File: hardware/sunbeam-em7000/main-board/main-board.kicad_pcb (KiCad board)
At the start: 4 copper layers, 131 x 125 mm, 0 parts

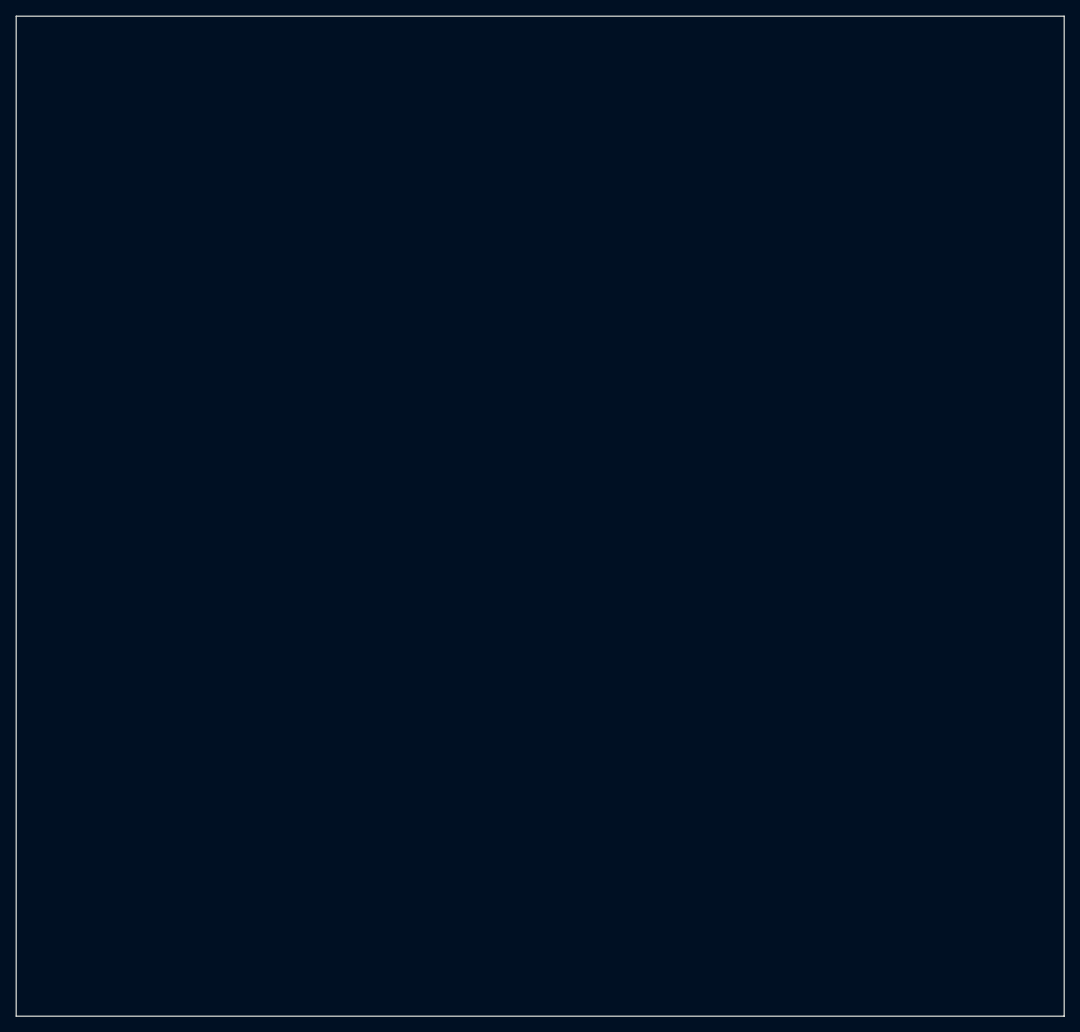
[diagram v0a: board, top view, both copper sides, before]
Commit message: main-board: placement candidate 1 [SOL-HW-MAIN-BOARD-PROVEN-AND-LAID-OUT.C7, .C18]
The first board branch's chosen placement (its candidate 5, 2f172f3a: candidate 4's mains-side moves and
TP202 at (71.5, 113.75)) replayed on this branch's floorplan, with the pump triacs T701 and T711 on the
board's two-lead DPAK land main-board:TO-252-2_TabPin2_Triac (swapped by KiCad's Python, keeping position,
turn, side, symbol link, fields and every pad's net, pin type and function; refilled and saved twice,
byte-identical). Every other footprint is the earlier board's, byte for byte in content.

Recorded as a candidate, not to be chosen: on the corrected floorplan the zero-crossing parts it leaves in
the old island (U602, R630, R631, TP103) stand in digital, outside the regions that list them.

The separation basis follows the land in the same commit (C18): the four entries that excused the 1.08 mm
gap of a middle-lead pad 2 against pads 1 and 3 are removed, since the land has no such pad; the tab pad
stands 2.00 mm from each lead pad, which meets the 2.0 mm terminal clearance and falls short of the 2.6 mm
creepage, so four creepage between entries at 2.0 mm take their place, unsigned (accepted_by and
accepted_on empty). The record's land and pin-distance comments, the division record's two restatements
and the record tests that pinned the 1.08 mm entries are brought to the land.

Co-Authored-By: Claude Sonnet 5.5 <noreply@anthropic.com>
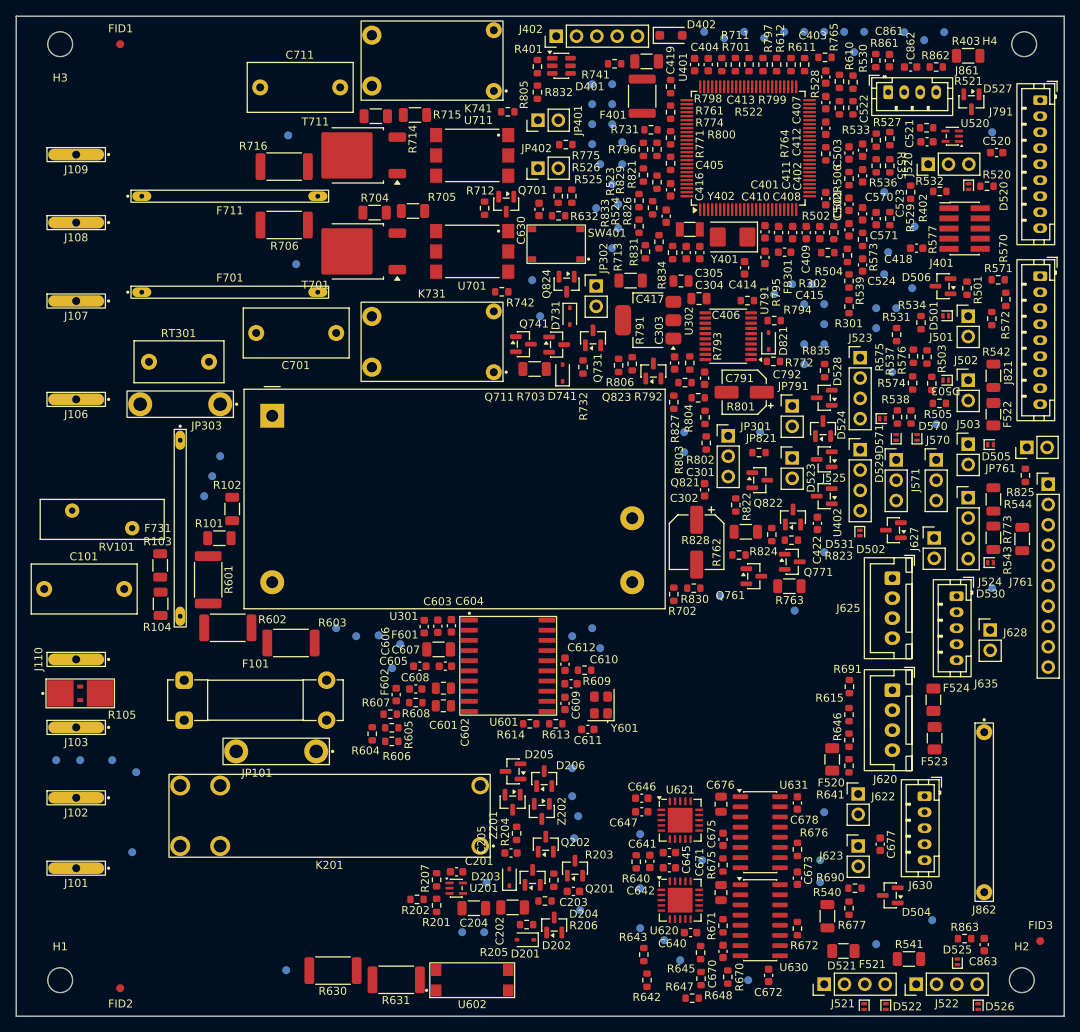
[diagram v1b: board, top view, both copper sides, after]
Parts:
- added C101: 100nF_X2, Capacitor_THT:C_Rect_L13.0mm_W6.0mm_P10.00mm_FKS3_FKP3_MKS4, F.Cu at (14.5, 73.6)
- added C201: 100n, Capacitor_SMD:C_0603_1608Metric, F.Cu at (56.0, 109.0)
- added C202: 100n, Capacitor_SMD:C_1206_3216Metric, F.Cu at (63.0, 113.4)
- added C203: 4.7n, Capacitor_SMD:C_0603_1608Metric, F.Cu at (70.7, 111.4)
- added C204: 100n, Capacitor_SMD:C_1206_3216Metric, F.Cu at (58.2, 113.5)
- added C205: 4.7n, Capacitor_SMD:C_0603_1608Metric, F.Cu at (62.9, 106.6)
- added C301: 100 nF, Capacitor_SMD:C_0603_1608Metric, F.Cu at (87.0, 61.2)
- added C302: 47 uF, Capacitor_SMD:CP_Elec_6.3x5.2, F.Cu at (86.0, 67.8)
- added C303: 10 uF, Capacitor_SMD:C_0603_1608Metric, F.Cu at (83.3, 45.4)
- added C304: 22 uF, Capacitor_SMD:C_0805_2012Metric, F.Cu at (86.3, 37.3)
- added C305: 22 uF, Capacitor_SMD:C_0805_2012Metric, F.Cu at (84.1, 35.1)
- added C401: 100 nF, Capacitor_SMD:C_0603_1608Metric, F.Cu at (94.6, 28.9)
- added C402: 100 nF, Capacitor_SMD:C_0603_1608Metric, F.Cu at (102.2, 24.8)
- added C403: 100 nF, Capacitor_SMD:C_0603_1608Metric, F.Cu at (102.2, 9.60)
- added C404: 100 nF, Capacitor_SMD:C_0603_1608Metric, F.Cu at (85.8, 8.05)
- added C405: 100 nF, Capacitor_SMD:C_0603_1608Metric, F.Cu at (82.8, 23.7)
- added C406: 100 nF, Capacitor_SMD:C_0603_1608Metric, F.Cu at (86.5, 31.6)
- added C407: 4.7 uF, Capacitor_SMD:C_0603_1608Metric, F.Cu at (102.2, 12.8)
- added C408: 100 nF, Capacitor_SMD:C_0603_1608Metric, F.Cu at (101.5, 29.1)
- added C409: 1 uF, Capacitor_SMD:C_0603_1608Metric, F.Cu at (99.8, 29.1)
- added C410: 100 nF, Capacitor_SMD:C_0603_1608Metric, F.Cu at (98.0, 29.1)
- added C411: 1 uF, Capacitor_SMD:C_0603_1608Metric, F.Cu at (96.3, 29.1)
- added C412: 2.2 uF, Capacitor_SMD:C_0603_1608Metric, F.Cu at (102.2, 16.0)
- added C413: 2.2 uF, Capacitor_SMD:C_0603_1608Metric, F.Cu at (87.5, 8.05)
- added C414: 20 pF, Capacitor_SMD:C_0603_1608Metric, F.Cu at (92.0, 33.5)
- added C415: 20 pF, Capacitor_SMD:C_0603_1608Metric, F.Cu at (94.6, 32.1)
- added C416: 4.7 pF, Capacitor_SMD:C_0603_1608Metric, F.Cu at (82.2, 27.0)
- added C417: 4.7 pF, Capacitor_SMD:C_0603_1608Metric, F.Cu at (84.8, 31.6)
- added C418: 100 nF, Capacitor_SMD:C_0603_1608Metric, F.Cu at (113.5, 31.0)
- added C419: 4.7 nF, Capacitor_SMD:C_1206_3216Metric, F.Cu at (79.8, 7.65)
- added C422: 100 nF, Capacitor_SMD:C_0603_1608Metric, F.Cu at (101.2, 65.4)
- added C501: 47n, Capacitor_SMD:C_0603_1608Metric, F.Cu at (105.1, 25.5)
- added C502: 47n, Capacitor_SMD:C_0603_1608Metric, F.Cu at (105.1, 28.7)
- added C503: 47n, Capacitor_SMD:C_0603_1608Metric, F.Cu at (105.1, 19.1)
- added C520: 47n, Capacitor_SMD:C_0603_1608Metric, F.Cu at (123.5, 19.1)
- added C521: 100n, Capacitor_SMD:C_0603_1608Metric, F.Cu at (114.8, 17.7)
- added C522: 47n, Capacitor_SMD:C_0603_1608Metric, F.Cu at (106.8, 18.8)
- added C523: 47n, Capacitor_SMD:C_0603_1608Metric, F.Cu at (106.8, 21.9)
- added C524: 47n, Capacitor_SMD:C_0603_1608Metric, F.Cu at (106.8, 33.1)
- added C570: 47n, Capacitor_SMD:C_0603_1608Metric, F.Cu at (106.8, 26.7)
- added C571: 47n, Capacitor_SMD:C_0603_1608Metric, F.Cu at (108.5, 27.3)
- added C601: 4.7n, Capacitor_SMD:C_0805_2012Metric, F.Cu at (54.4, 88.2)
- added C602: 4.7n, Capacitor_SMD:C_0805_2012Metric, F.Cu at (54.4, 86.0)
- added C603: 1u, Capacitor_SMD:C_0603_1608Metric, F.Cu at (53.7, 78.2)
- added C604: 1n, Capacitor_SMD:C_0603_1608Metric, F.Cu at (55.4, 78.2)
- added C605: 100n, Capacitor_SMD:C_0603_1608Metric, F.Cu at (51.5, 83.2)
- added C606: 1n, Capacitor_SMD:C_0603_1608Metric, F.Cu at (54.6, 83.2)
- added C607: 100n, Capacitor_SMD:C_1206_3216Metric, F.Cu at (53.8, 81.2)
- added C608: 1n, Capacitor_SMD:C_0603_1608Metric, F.Cu at (51.0, 86.1)
- added C609: 1n, Capacitor_SMD:C_0603_1608Metric, F.Cu at (69.6, 87.9)
- added C610: 1u, Capacitor_SMD:C_0603_1608Metric, F.Cu at (70.3, 85.5)
- added C611: 100n, Capacitor_SMD:C_0603_1608Metric, F.Cu at (72.5, 91.2)
- added C612: 100n, Capacitor_SMD:C_0603_1608Metric, F.Cu at (69.6, 83.0)
- added C630: 1n, Capacitor_SMD:C_0603_1608Metric, F.Cu at (66.3, 26.1)
- added C640: 10n, Capacitor_SMD:C_0603_1608Metric, F.Cu at (85.3, 116.5)
- added C641: 100n, Capacitor_SMD:C_0603_1608Metric, F.Cu at (80.2, 107.7)
- added C642: 100n, Capacitor_SMD:C_0603_1608Metric, F.Cu at (82.7, 108.5)
- added C645: 10n, Capacitor_SMD:C_0603_1608Metric, F.Cu at (82.7, 106.5)
- added C646: 100n, Capacitor_SMD:C_0603_1608Metric, F.Cu at (79.2, 99.8)
- added C647: 100n, Capacitor_SMD:C_0603_1608Metric, F.Cu at (79.2, 101.5)
- added C670: 100n, Capacitor_SMD:C_0603_1608Metric, F.Cu at (89.3, 118.9)
- added C671: 10u, Capacitor_SMD:C_0805_2012Metric, F.Cu at (89.1, 111.5)
- added C672: 100n, Capacitor_SMD:C_0603_1608Metric, F.Cu at (95.0, 121.9)
- added C673: 100n, Capacitor_SMD:C_0603_1608Metric, F.Cu at (98.7, 109.8)
- added C675: 100n, Capacitor_SMD:C_0603_1608Metric, F.Cu at (89.3, 104.9)
- added C676: 10u, Capacitor_SMD:C_0805_2012Metric, F.Cu at (89.1, 100.5)
- added C677: 100n, Capacitor_SMD:C_0603_1608Metric, F.Cu at (109.0, 105.5)
- added C678: 100n, Capacitor_SMD:C_0603_1608Metric, F.Cu at (98.7, 100.3)
- added C701: 100nF_X2, Capacitor_THT:C_Rect_L13.0mm_W6.0mm_P10.00mm_FKS3_FKP3_MKS4, F.Cu at (41.0, 41.6)
- added C711: 100nF_X2, Capacitor_THT:C_Rect_L13.0mm_W6.0mm_P10.00mm_FKS3_FKP3_MKS4, F.Cu at (41.5, 10.9)
- added C791: 100n, Capacitor_SMD:C_0603_1608Metric, F.Cu at (87.0, 47.2)
- added C792: 47u, Capacitor_SMD:CP_Elec_5x5.4, F.Cu at (92.0, 49.0)
- added C861: 100n, Capacitor_SMD:C_0603_1608Metric, F.Cu at (110.2, 7.55)
- added C862: 100n, Capacitor_SMD:C_0603_1608Metric, F.Cu at (112.8, 8.35)
- added C863: 100n, Capacitor_SMD:C_0603_1608Metric, F.Cu at (122.0, 118.0)
- added D201: BAT54HT1G, Diode_SMD:D_SOD-323, F.Cu at (64.7, 117.5)
- added D202: BAS116, Package_TO_SOT_SMD:SOT-23, F.Cu at (68.2, 115.6)
- added D203: BAT54HT1G, Diode_SMD:D_SOD-323, F.Cu at (62.6, 109.7)
- added D204: BAS116, Package_TO_SOT_SMD:SOT-23, F.Cu at (65.5, 109.7)
- added D205: BAS116, Package_TO_SOT_SMD:SOT-23, F.Cu at (63.1, 96.4)
- added D206: BAS116, Package_TO_SOT_SMD:SOT-23, F.Cu at (67.0, 97.3)
- added D401: USBLC6-2SC6, Package_TO_SOT_SMD:SOT-23-6, F.Cu at (69.2, 8.20)
- added D402: SMF6.0A, Diode_SMD:D_SOD-123F, F.Cu at (82.8, 4.40)
- added D501: PESD5V0F1BL, Diode_SMD:D_SOD-882, F.Cu at (117.2, 39.5)
- added D502: BAT54S, Package_TO_SOT_SMD:SOT-23, F.Cu at (110.7, 66.2)
- added D503: PESD5V0F1BL, Diode_SMD:D_SOD-882, F.Cu at (117.2, 47.5)
- added D504: BAT54S, Package_TO_SOT_SMD:SOT-23, F.Cu at (110.2, 111.9)
- added D505: PESD5V0F1BL, Diode_SMD:D_SOD-882, F.Cu at (122.8, 55.5)
- added D506: BAT54S, Package_TO_SOT_SMD:SOT-23, F.Cu at (116.8, 35.8)
- added D520: PESD5V0F1BL, Diode_SMD:D_SOD-882, F.Cu at (120.0, 23.3)
- added D521: PESD5V0F1BL, Diode_SMD:D_SOD-882, F.Cu at (107.0, 125.8)
- added D522: PESD5V0F1BL, Diode_SMD:D_SOD-882, F.Cu at (109.7, 125.8)
- added D523: BAT54S, Package_TO_SOT_SMD:SOT-23, F.Cu at (101.8, 53.5)
- added D524: BAT54S, Package_TO_SOT_SMD:SOT-23, F.Cu at (102.0, 57.4)
- added D525: PESD5V0F1BL, Diode_SMD:D_SOD-882, F.Cu at (118.7, 120.2)
- added D526: PESD5V0F1BL, Diode_SMD:D_SOD-882, F.Cu at (121.2, 125.8)
- added D527: BAT54S, Package_TO_SOT_SMD:SOT-23, F.Cu at (120.4, 12.7)
- added D528: BAT54S, Package_TO_SOT_SMD:SOT-23, F.Cu at (102.0, 49.7)
- added D529: PESD5V0F1BL, Diode_SMD:D_SOD-882, F.Cu at (109.3, 52.3)
- added D530: PESD5V0F1BL, Diode_SMD:D_SOD-882, F.Cu at (122.8, 70.3)
- added D531: PESD5V0F1BL, Diode_SMD:D_SOD-882, F.Cu at (106.5, 66.6)
- added D570: PESD5V0F1BL, Diode_SMD:D_SOD-882, F.Cu at (113.6, 54.6)
- added D571: PESD5V0F1BL, Diode_SMD:D_SOD-882, F.Cu at (111.0, 54.6)
- added D731: 1N4148WS, Diode_SMD:D_SOD-323, F.Cu at (70.2, 39.5)
- added D741: 1N4148WS, Diode_SMD:D_SOD-323, F.Cu at (69.3, 46.6)
- added D821: 1N4148WS, Diode_SMD:D_SOD-323, F.Cu at (95.0, 42.6)
- added F101: 10A_T_250V, Fuse:Fuseholder_Clip-5x20mm_Bel_FC-203-22_Lateral_P17.80x5.00mm_D1.17mm_Horizontal, F.Cu at (22.0, 85.0)
- added F401: MF-MSMF050-2, Fuse:Fuse_1812_4532Metric, F.Cu at (79.2, 12.0)
- added F520: MF-NSMF012-2, Fuse:Fuse_1206_3216Metric, F.Cu at (103.0, 94.9)
- added F521: MF-NSMF012-2, Fuse:Fuse_1206_3216Metric, F.Cu at (104.4, 118.8)
- added F522: MF-NSMF012-2, Fuse:Fuse_1206_3216Metric, F.Cu at (123.2, 51.8)
- added F523: MF-NSMF012-2, Fuse:Fuse_1206_3216Metric, F.Cu at (115.8, 92.2)
- added F524: MF-NSMF012-2, Fuse:Fuse_1206_3216Metric, F.Cu at (115.7, 87.5)
- added F601: 600R@100MHz, Inductor_SMD:L_0603_1608Metric, F.Cu at (52.0, 78.3)
- added F602: 600R@100MHz, Inductor_SMD:L_0603_1608Metric, F.Cu at (48.5, 86.8)
- added F701: 0.8A, main-board:FUSEHOLDER_5x20_XC_BLX-A, F.Cu at (27.7, 36.5)
- added F711: 0.5A, main-board:FUSEHOLDER_5x20_XC_BLX-A, F.Cu at (27.7, 24.5)
- added F731: 0.4A, main-board:FUSEHOLDER_5x20_XC_BLX-A, F.Cu at (21.5, 66.0)
- added FB301: 600R@100MHz, Inductor_SMD:L_0603_1608Metric, F.Cu at (97.0, 31.5)
- added FID1: Fiducial, Fiducial:Fiducial_1mm_Mask2mm, F.Cu at (14.0, 5.50)
- added FID2: Fiducial, Fiducial:Fiducial_1mm_Mask2mm, F.Cu at (14.0, 123.5)
- added FID3: Fiducial, Fiducial:Fiducial_1mm_Mask2mm, F.Cu at (129.0, 117.6)
- added H1: MountingHole, main-board:MountingHole_3.1mm_Lid, F.Cu at (6.50, 122.5)
- added H2: MountingHole, main-board:MountingHole_3.1mm_Lid, F.Cu at (126.7, 122.5)
- added H3: MountingHole, main-board:MountingHole_3.1mm_Lid, F.Cu at (6.50, 5.50)
- added H4: MountingHole, main-board:MountingHole_3.1mm_Lid, F.Cu at (127.0, 5.50)
- added J101: TAB1_LINE1, main-board:Tab_BZXC_BTC-3-PCB634908T, F.Cu at (8.50, 108.5)
- added J102: TAB2_LINE_IN, main-board:Tab_BZXC_BTC-3-PCB634908T, F.Cu at (8.50, 99.7)
- added J103: TAB3_NEUTRAL_IN, main-board:Tab_BZXC_BTC-3-PCB634908T, F.Cu at (8.50, 90.9)
- added J106: TAB6_COFVALVE, main-board:Tab_BZXC_BTC-3-PCB634908T, F.Cu at (8.50, 49.9)
- added J107: TAB7_COFFPUMP, main-board:Tab_BZXC_BTC-3-PCB634908T, F.Cu at (8.50, 37.6)
- added J108: TAB8_STEAMPUMP, main-board:Tab_BZXC_BTC-3-PCB634908T, F.Cu at (8.50, 27.8)
- added J109: TAB9_HOTVALVE, main-board:Tab_BZXC_BTC-3-PCB634908T, F.Cu at (8.50, 19.3)
- added J110: WB_RET, main-board:Tab_BZXC_BTC-3-PCB634908T, F.Cu at (8.50, 82.4)
- added J401: SWD, Connector_PinHeader_1.27mm:PinHeader_2x05_P1.27mm_Vertical_SMD, F.Cu at (119.5, 28.5)
- added J402: USB_PANEL, Connector_PinHeader_2.54mm:PinHeader_1x05_P2.54mm_Vertical, F.Cu at (68.5, 4.50)
- added J501: TEMP_C, Connector_PinHeader_2.54mm:PinHeader_1x02_P2.54mm_Vertical, F.Cu at (120.0, 39.5)
- added J502: TEMP_S, Connector_PinHeader_2.54mm:PinHeader_1x02_P2.54mm_Vertical, F.Cu at (120.0, 47.5)
- added J503: TEMP_W, Connector_PinHeader_2.54mm:PinHeader_1x02_P2.54mm_Vertical, F.Cu at (120.0, 55.5)
- added J520: FLOW, Connector_PinHeader_2.54mm:PinHeader_1x03_P2.54mm_Vertical, F.Cu at (115.0, 20.5)
- added J521: STM_D, Connector_PinHeader_2.54mm:PinHeader_1x04_P2.54mm_Vertical, F.Cu at (102.0, 123.0)
- added J522: BREW_D, Connector_PinHeader_2.54mm:PinHeader_1x04_P2.54mm_Vertical, F.Cu at (113.5, 123.0)
- added J523: SPARE_A, Connector_PinHeader_2.54mm:PinHeader_1x04_P2.54mm_Vertical, F.Cu at (106.5, 44.7)
- added J524: BREW_A, Connector_PinHeader_2.54mm:PinHeader_1x04_P2.54mm_Vertical, F.Cu at (120.0, 62.2)
- added J525: SPARE_AN2_H, Connector_PinHeader_2.54mm:PinHeader_1x04_P2.54mm_Vertical, F.Cu at (106.5, 56.2)
- added J570: CURR1_H, Connector_PinHeader_2.54mm:PinHeader_1x03_P2.54mm_Vertical, F.Cu at (116.0, 57.5)
- added J571: CURR2_H, Connector_PinHeader_2.54mm:PinHeader_1x03_P2.54mm_Vertical, F.Cu at (111.0, 57.5)
- added J620: PT1_H, Connector_JST:JST_XH_B4B-XH-A_1x04_P2.50mm_Vertical, F.Cu at (110.5, 86.2)
- added J622: PT1_2W_P, Connector_PinHeader_2.54mm:PinHeader_1x02_P2.54mm_Vertical, F.Cu at (106.2, 99.2)
- added J623: PT1_23W_N, Connector_PinHeader_2.54mm:PinHeader_1x02_P2.54mm_Vertical, F.Cu at (106.2, 105.7)
- added J625: PT2_H, Connector_JST:JST_XH_B4B-XH-A_1x04_P2.50mm_Vertical, F.Cu at (110.5, 72.2)
- added J627: PT2_2W_P, Connector_PinHeader_2.54mm:PinHeader_1x02_P2.54mm_Vertical, F.Cu at (115.8, 67.2)
- added J628: PT2_23W_N, Connector_PinHeader_2.54mm:PinHeader_1x02_P2.54mm_Vertical, F.Cu at (122.8, 78.7)
- added J630: WT1_H, Connector_JST:JST_PH_B5B-PH-K_1x05_P2.00mm_Vertical, F.Cu at (114.5, 99.5)
- added J635: WT2_H, Connector_JST:JST_PH_B5B-PH-K_1x05_P2.00mm_Vertical, F.Cu at (118.5, 74.5)
- added J761: WB_LV10, Connector_PinHeader_2.54mm:PinHeader_1x10_P2.54mm_Vertical, F.Cu at (130.0, 60.5)
- added J791: SP2, Connector_JST:JST_PH_B9B-PH-K_1x09_P2.00mm_Vertical, F.Cu at (129.0, 12.5)
- added J821: CON2, Connector_JST:JST_PH_B9B-PH-K_1x09_P2.00mm_Vertical, F.Cu at (129.0, 34.5)
- added J861: KNOB, Connector_JST:JST_PH_B4B-PH-K_1x04_P2.00mm_Vertical, F.Cu at (110.0, 11.5)
- added J862: REED, main-board:REED_PADS_P20.00mm, F.Cu at (122.0, 91.5)
- added JP101: LINK_LIVE, main-board:JP101_WireLink_P10mm, F.Cu at (38.5, 93.9)
- added JP301: SEL_5V, Connector_PinHeader_2.54mm:PinHeader_1x03_P2.54mm_Vertical, F.Cu at (90.0, 54.5)
- added JP302: LINK_3V3, Connector_PinHeader_2.54mm:PinHeader_1x02_P2.54mm_Vertical, F.Cu at (73.5, 35.7)
- added JP303: LINK_MOD, main-board:JP101_WireLink_P10mm, F.Cu at (26.5, 50.5)
- added JP401: BOOT0_HI, Connector_PinHeader_2.54mm:PinHeader_1x02_P2.54mm_Vertical, F.Cu at (66.2, 15.0)
- added JP402: LINK_VTREF, Connector_PinHeader_2.54mm:PinHeader_1x02_P2.54mm_Vertical, F.Cu at (66.2, 21.0)
- added JP761: LINK, Connector_PinHeader_2.54mm:PinHeader_1x02_P2.54mm_Vertical, F.Cu at (127.3, 55.9)
- added JP791: LINK, Connector_PinHeader_2.54mm:PinHeader_1x02_P2.54mm_Vertical, F.Cu at (98.0, 50.7)
- added JP821: LINK, Connector_PinHeader_2.54mm:PinHeader_1x02_P2.54mm_Vertical, F.Cu at (98.0, 57.2)
- added K201: HF115F-Q/005-1H, main-board:Relay_HF115F-Q_1H_Vertical, F.Cu at (59.0, 105.7)
- added K731: HF32FA-G/005-HSL1, main-board:RELAY_HF32FA-G_1H_TYPE1_THT, F.Cu at (60.7, 46.5)
- added K741: HF32FA-G/005-HSL1, main-board:RELAY_HF32FA-G_1H_TYPE1_THT, F.Cu at (60.7, 11.3)
- added Q201: NX3008NBK, Package_TO_SOT_SMD:SOT-23, F.Cu at (70.8, 108.5)
- added Q202: NX3008NBK, Package_TO_SOT_SMD:SOT-23, F.Cu at (67.2, 105.5)
- added Q701: AO3400A, Package_TO_SOT_SMD:SOT-23, F.Cu at (62.2, 25.5)
- added Q711: AO3400A, Package_TO_SOT_SMD:SOT-23, F.Cu at (64.4, 43.0)
- added Q731: AO3400A, Package_TO_SOT_SMD:SOT-23, F.Cu at (73.1, 42.2)
- added Q741: AO3400A, Package_TO_SOT_SMD:SOT-23, F.Cu at (68.5, 43.0)
- added Q761: AO3400A, Package_TO_SOT_SMD:SOT-23, F.Cu at (93.2, 72.0)
- added Q771: AO3400A, Package_TO_SOT_SMD:SOT-23, F.Cu at (98.0, 70.2)
- added Q821: AO3400A, Package_TO_SOT_SMD:SOT-23, F.Cu at (94.0, 60.0)
- added Q822: AO3401A, Package_TO_SOT_SMD:SOT-23, F.Cu at (98.1, 64.6)
- added Q823: AO3400A, Package_TO_SOT_SMD:SOT-23, F.Cu at (80.7, 46.4)
- added Q824: AO3400A, Package_TO_SOT_SMD:SOT-23, F.Cu at (69.8, 35.5)
- added R101: 1Meg, Resistor_SMD:R_1206_3216Metric, F.Cu at (26.4, 67.2)
- added R102: 1Meg, Resistor_SMD:R_1206_3216Metric, F.Cu at (28.0, 63.6)
- added R103: 1Meg, Resistor_SMD:R_1206_3216Metric, F.Cu at (19.0, 70.7)
- added R104: 1Meg, Resistor_SMD:R_1206_3216Metric, F.Cu at (19.1, 75.5)
- added R105: 1m, main-board:R_WSK2512_4T, F.Cu at (9.00, 86.7)
- added R201: 100k, Resistor_SMD:R_0603_1608Metric, F.Cu at (53.5, 113.2)
- added R202: 100k, Resistor_SMD:R_0603_1608Metric, F.Cu at (51.1, 112.4)
- added R203: 5.6Meg, Resistor_SMD:R_0603_1608Metric, F.Cu at (68.2, 110.0)
- added R204: 5.6Meg, Resistor_SMD:R_0603_1608Metric, F.Cu at (63.5, 104.2)
- added R205: 100k, Resistor_SMD:R_0603_1608Metric, F.Cu at (64.8, 115.5)
- added R206: 100k, Resistor_SMD:R_0603_1608Metric, F.Cu at (67.1, 112.6)
- added R207: 1k, Resistor_SMD:R_0603_1608Metric, F.Cu at (53.5, 110.0)
- added R301: 0, Resistor_SMD:R_0603_1608Metric, F.Cu at (105.1, 38.3)
- added R302: 0, Resistor_SMD:R_0603_1608Metric, F.Cu at (102.5, 31.6)
- added R401: 10k, Resistor_SMD:R_0603_1608Metric, F.Cu at (66.2, 8.30)
- added R402: 1k, Resistor_SMD:R_0603_1608Metric, F.Cu at (116.5, 23.9)
- added R403: 1Meg, Resistor_SMD:R_1206_3216Metric, F.Cu at (120.0, 6.95)
- added R501: 10k, Resistor_SMD:R_0603_1608Metric, F.Cu at (119.8, 36.0)
- added R502: 1k, Resistor_SMD:R_0603_1608Metric, F.Cu at (103.2, 29.1)
- added R503: 10k, Resistor_SMD:R_0603_1608Metric, F.Cu at (115.5, 47.9)
- added R504: 1k, Resistor_SMD:R_0603_1608Metric, F.Cu at (104.9, 31.9)
- added R505: 10k, Resistor_SMD:R_0603_1608Metric, F.Cu at (116.4, 50.4)
- added R506: 1k, Resistor_SMD:R_0603_1608Metric, F.Cu at (105.1, 22.3)
- added R520: 10k, Resistor_SMD:R_0603_1608Metric, F.Cu at (122.3, 23.2)
- added R521: 1k, Resistor_SMD:R_0603_1608Metric, F.Cu at (114.8, 15.9)
- added R522: 0, Resistor_SMD:R_0603_1608Metric, F.Cu at (92.6, 8.05)
- added R523: 100, Resistor_SMD:R_0603_1608Metric, F.Cu at (81.1, 22.8)
- added R524: 100, Resistor_SMD:R_0603_1608Metric, F.Cu at (80.5, 25.9)
- added R525: 2.2k, Resistor_SMD:R_0603_1608Metric, F.Cu at (70.5, 24.5)
- added R526: 2.2k, Resistor_SMD:R_0603_1608Metric, F.Cu at (68.8, 24.5)
- added R527: 100, Resistor_SMD:R_0603_1608Metric, F.Cu at (103.9, 13.4)
- added R528: 100, Resistor_SMD:R_0603_1608Metric, F.Cu at (105.6, 13.4)
- added R529: 2.2k, Resistor_SMD:R_0603_1608Metric, F.Cu at (112.8, 24.0)
- added R530: 2.2k, Resistor_SMD:R_0603_1608Metric, F.Cu at (105.6, 10.2)
- added R531: 10k, Resistor_SMD:R_0603_1608Metric, F.Cu at (111.0, 41.8)
- added R532: 20k, Resistor_SMD:R_0603_1608Metric, F.Cu at (110.2, 17.3)
- added R533: 1k, Resistor_SMD:R_0603_1608Metric, F.Cu at (108.5, 17.5)
- added R534: 10k, Resistor_SMD:R_0603_1608Metric, F.Cu at (114.1, 40.3)
- added R535: 20k, Resistor_SMD:R_0603_1608Metric, F.Cu at (110.2, 20.7)
- added R536: 1k, Resistor_SMD:R_0603_1608Metric, F.Cu at (108.5, 20.7)
- added R537: 10k, Resistor_SMD:R_0603_1608Metric, F.Cu at (111.2, 52.1)
- added R538: 20k, Resistor_SMD:R_0603_1608Metric, F.Cu at (112.8, 52.1)
- added R539: 1k, Resistor_SMD:R_0603_1608Metric, F.Cu at (105.1, 35.1)
- added R540: 0, Resistor_SMD:R_1206_3216Metric, F.Cu at (102.4, 114.5)
- added R541: 0, Resistor_SMD:R_1206_3216Metric, F.Cu at (112.6, 119.8)
- added R542: 0, Resistor_SMD:R_1206_3216Metric, F.Cu at (123.2, 47.0)
- added R543: 0, Resistor_SMD:R_1206_3216Metric, F.Cu at (123.2, 67.2)
- added R544: 0, Resistor_SMD:R_1206_3216Metric, F.Cu at (123.2, 62.4)
- added R570: 10k, Resistor_SMD:R_0603_1608Metric, F.Cu at (123.0, 39.8)
- added R571: 20k, Resistor_SMD:R_0603_1608Metric, F.Cu at (123.8, 35.0)
- added R572: DNP, Resistor_SMD:R_0603_1608Metric, F.Cu at (124.7, 37.4)
- added R573: 1k, Resistor_SMD:R_0603_1608Metric, F.Cu at (106.8, 29.9)
- added R574: 10k, Resistor_SMD:R_0603_1608Metric, F.Cu at (113.0, 47.9)
- added R575: 20k, Resistor_SMD:R_0603_1608Metric, F.Cu at (114.8, 44.6)
- added R576: DNP, Resistor_SMD:R_0603_1608Metric, F.Cu at (113.2, 44.5)
- added R577: 1k, Resistor_SMD:R_0603_1608Metric, F.Cu at (110.2, 27.3)
- added R601: 300k, Resistor_SMD:R_2512_6332Metric, F.Cu at (25.0, 72.5)
- added R602: 300k, Resistor_SMD:R_2512_6332Metric, F.Cu at (27.4, 78.5)
- added R603: 300k, Resistor_SMD:R_2512_6332Metric, F.Cu at (35.4, 80.3)
- added R604: 750, Resistor_SMD:R_0603_1608Metric, F.Cu at (45.5, 91.7)
- added R605: 49.9, Resistor_SMD:R_0603_1608Metric, F.Cu at (48.0, 91.0)
- added R606: 49.9, Resistor_SMD:R_0603_1608Metric, F.Cu at (48.0, 92.7)
- added R607: 330, Resistor_SMD:R_0603_1608Metric, F.Cu at (47.8, 89.2)
- added R608: 330, Resistor_SMD:R_0603_1608Metric, F.Cu at (51.0, 87.8)
- added R609: 33, Resistor_SMD:R_0603_1608Metric, F.Cu at (72.0, 83.8)
- added R610: 33, Resistor_SMD:R_0603_1608Metric, F.Cu at (103.9, 10.2)
- added R611: 33, Resistor_SMD:R_0603_1608Metric, F.Cu at (99.5, 8.05)
- added R612: 33, Resistor_SMD:R_0603_1608Metric, F.Cu at (97.8, 8.05)
- added R613: 33, Resistor_SMD:R_0603_1608Metric, F.Cu at (68.5, 90.5)
- added R614: 100k, Resistor_SMD:R_0603_1608Metric, F.Cu at (65.2, 90.5)
- added R615: 100k, Resistor_SMD:R_0603_1608Metric, F.Cu at (105.1, 89.3)
- added R630: 60.4k, Resistor_SMD:R_2512_6332Metric, F.Cu at (40.6, 121.3)
- added R631: 60.4k, Resistor_SMD:R_2512_6332Metric, F.Cu at (48.5, 122.5)
- added R632: 22k, Resistor_SMD:R_0603_1608Metric, F.Cu at (68.8, 26.9)
- added R640: 4.02k, Resistor_SMD:R_0603_1608Metric, F.Cu at (78.5, 107.7)
- added R641: 100k, Resistor_SMD:R_0603_1608Metric, F.Cu at (105.1, 95.7)
- added R642: 0, Resistor_SMD:R_0603_1608Metric, F.Cu at (79.8, 122.5)
- added R643: 0, Resistor_SMD:R_0603_1608Metric, F.Cu at (79.5, 119.3)
- added R645: 4.02k, Resistor_SMD:R_0603_1608Metric, F.Cu at (86.5, 119.0)
- added R646: 100k, Resistor_SMD:R_0603_1608Metric, F.Cu at (105.1, 92.5)
- added R647: 0, Resistor_SMD:R_0603_1608Metric, F.Cu at (85.5, 124.8)
- added R648: 0, Resistor_SMD:R_0603_1608Metric, F.Cu at (86.6, 122.3)
- added R670: 100, Resistor_SMD:R_0603_1608Metric, F.Cu at (90.0, 122.1)
- added R671: 100, Resistor_SMD:R_0603_1608Metric, F.Cu at (89.3, 115.7)
- added R672: 100k, Resistor_SMD:R_0603_1608Metric, F.Cu at (98.7, 116.0)
- added R675: 100, Resistor_SMD:R_0603_1608Metric, F.Cu at (89.3, 108.1)
- added R676: 100, Resistor_SMD:R_0603_1608Metric, F.Cu at (98.7, 106.2)
- added R677: 100k, Resistor_SMD:R_0603_1608Metric, F.Cu at (105.1, 113.5)
- added R690: 0, Resistor_SMD:R_0603_1608Metric, F.Cu at (105.8, 111.0)
- added R691: 0, Resistor_SMD:R_0603_1608Metric, F.Cu at (105.2, 85.8)
- added R701: 100, Resistor_SMD:R_0603_1608Metric, F.Cu at (89.2, 8.05)
- added R702: 100k, Resistor_SMD:R_0603_1608Metric, F.Cu at (83.2, 74.2)
- added R703: 180, Resistor_SMD:R_1206_3216Metric, F.Cu at (65.8, 46.1)
- added R704: 200, Resistor_SMD:R_1206_3216Metric, F.Cu at (45.8, 26.6)
- added R705: 200, Resistor_SMD:R_1206_3216Metric, F.Cu at (50.6, 26.4)
- added R706: 100, Resistor_SMD:R_2512_6332Metric, F.Cu at (34.5, 28.1)
- added R711: 100, Resistor_SMD:R_0603_1608Metric, F.Cu at (90.9, 8.05)
- added R712: 100k, Resistor_SMD:R_0603_1608Metric, F.Cu at (59.5, 26.0)
- added R713: 180, Resistor_SMD:R_1206_3216Metric, F.Cu at (77.8, 35.0)
- added R714: 200, Resistor_SMD:R_1206_3216Metric, F.Cu at (46.0, 14.5)
- added R715: 200, Resistor_SMD:R_1206_3216Metric, F.Cu at (50.9, 14.3)
- added R716: 100, Resistor_SMD:R_2512_6332Metric, F.Cu at (34.5, 20.8)
- added R731: 100, Resistor_SMD:R_0603_1608Metric, F.Cu at (80.3, 16.2)
- added R732: 100k, Resistor_SMD:R_0603_1608Metric, F.Cu at (71.8, 45.9)
- added R741: 100, Resistor_SMD:R_0603_1608Metric, F.Cu at (75.8, 7.95)
- added R742: 100k, Resistor_SMD:R_0603_1608Metric, F.Cu at (61.7, 36.5)
- added R761: 100, Resistor_SMD:R_0603_1608Metric, F.Cu at (82.8, 17.2)
- added R762: 100k, Resistor_SMD:R_0603_1608Metric, F.Cu at (91.3, 69.3)
- added R763: 180, Resistor_SMD:R_1206_3216Metric, F.Cu at (97.7, 73.2)
- added R764: 27k, Resistor_SMD:R_0603_1608Metric, F.Cu at (102.2, 19.2)
- added R765: 82k, Resistor_SMD:R_0603_1608Metric, F.Cu at (102.1, 7.15)
- added R771: 100, Resistor_SMD:R_0603_1608Metric, F.Cu at (81.1, 18.6)
- added R772: 100k, Resistor_SMD:R_0603_1608Metric, F.Cu at (95.7, 45.1)
- added R773: 180, Resistor_SMD:R_1206_3216Metric, F.Cu at (126.8, 67.3)
- added R774: 27k, Resistor_SMD:R_0603_1608Metric, F.Cu at (82.8, 20.4)
- added R775: 82k, Resistor_SMD:R_0603_1608Metric, F.Cu at (69.7, 18.1)
- added R791: 100, Resistor_SMD:R_0603_1608Metric, F.Cu at (78.0, 45.5)
- added R792: 100, Resistor_SMD:R_0603_1608Metric, F.Cu at (84.6, 47.8)
- added R793: 100, Resistor_SMD:R_0603_1608Metric, F.Cu at (85.2, 45.4)
- added R794: 100, Resistor_SMD:R_0603_1608Metric, F.Cu at (95.8, 40.0)
- added R795: 100, Resistor_SMD:R_0603_1608Metric, F.Cu at (92.4, 37.5)
- added R796: 1k, Resistor_SMD:R_0603_1608Metric, F.Cu at (79.4, 18.6)
- added R797: 1k, Resistor_SMD:R_0603_1608Metric, F.Cu at (96.0, 8.05)
- added R798: 1k, Resistor_SMD:R_0603_1608Metric, F.Cu at (82.8, 10.8)
- added R799: 1k, Resistor_SMD:R_0603_1608Metric, F.Cu at (94.3, 8.05)
- added R800: 1k, Resistor_SMD:R_0603_1608Metric, F.Cu at (82.8, 14.0)
- added R801: 10k, Resistor_SMD:R_0603_1608Metric, F.Cu at (93.8, 56.5)
- added R802: 10k, Resistor_SMD:R_0603_1608Metric, F.Cu at (87.2, 55.4)
- added R803: 10k, Resistor_SMD:R_0603_1608Metric, F.Cu at (87.1, 52.1)
- added R804: 10k, Resistor_SMD:R_0603_1608Metric, F.Cu at (86.2, 49.7)
- added R805: 10k, Resistor_SMD:R_0603_1608Metric, F.Cu at (62.5, 13.9)
- added R806: 10k, Resistor_SMD:R_0603_1608Metric, F.Cu at (76.3, 45.6)
- added R821: 100, Resistor_SMD:R_0603_1608Metric, F.Cu at (79.4, 21.9)
- added R822: 100k, Resistor_SMD:R_0603_1608Metric, F.Cu at (91.0, 63.1)
- added R823: 22k, Resistor_SMD:R_0603_1608Metric, F.Cu at (97.9, 67.5)
- added R824: 22k, Resistor_SMD:R_0603_1608Metric, F.Cu at (95.5, 66.8)
- added R825: 22k, Resistor_SMD:R_0603_1608Metric, F.Cu at (127.2, 59.4)
- added R826: 100, Resistor_SMD:R_0603_1608Metric, F.Cu at (78.8, 28.2)
- added R827: 100k, Resistor_SMD:R_0603_1608Metric, F.Cu at (83.2, 50.2)
- added R828: 100, Resistor_SMD:R_1206_3216Metric, F.Cu at (92.2, 66.5)
- added R829: 100, Resistor_SMD:R_0603_1608Metric, F.Cu at (78.8, 25.1)
- added R830: 100k, Resistor_SMD:R_0603_1608Metric, F.Cu at (85.7, 73.5)
- added R831: 10k, Resistor_SMD:R_0603_1608Metric, F.Cu at (79.7, 31.4)
- added R832: 10k, Resistor_SMD:R_0603_1608Metric, F.Cu at (66.2, 11.5)
- added R833: 10k, Resistor_SMD:R_0603_1608Metric, F.Cu at (81.3, 30.2)
- added R834: 10k, Resistor_SMD:R_0603_1608Metric, F.Cu at (83.0, 31.6)
- added R835: 10k, Resistor_SMD:R_0603_1608Metric, F.Cu at (102.0, 46.3)
- added R861: 10k, Resistor_SMD:R_0603_1608Metric, F.Cu at (108.5, 7.55)
- added R862: 10k, Resistor_SMD:R_0603_1608Metric, F.Cu at (116.0, 8.35)
- added R863: 10k, Resistor_SMD:R_0603_1608Metric, F.Cu at (119.5, 117.3)
- added RT301: NTC 10D-9, Capacitor_THT:C_Disc_D11.0mm_W5.0mm_P7.50mm, F.Cu at (17.6, 45.2)
- added RV101: 14D471K, Varistor:RV_Disc_D15.5mm_W5mm_P7.5mm, F.Cu at (15.5, 66.0)
- added SW401: RESET, main-board:TS1187A_5.1x5.1mm_SMD, F.Cu at (68.5, 30.5)
- added T701: BTA204S-600B, main-board:TO-252-2_TabPin2_Triac, F.Cu at (43.6, 31.4)
- added T711: BTA204S-600B, main-board:TO-252-2_TabPin2_Triac, F.Cu at (43.6, 19.4)
- added TP101: TP_LINE_IN, main-board:TestPoint_Pad_D1.0mm_Tight, B.Cu at (16.0, 96.5)
- added TP102: TP_LINE_F, main-board:TestPoint_Pad_D1.0mm_Tight, B.Cu at (13.0, 95.0)
- added TP103: TP_LINE, main-board:TestPoint_Pad_D1.0mm_Tight, B.Cu at (34.8, 121.2)
- added TP104: TP_LINE1, main-board:TestPoint_Pad_D1.0mm_Tight, B.Cu at (15.5, 106.5)
- added TP105: TP_NEUTRAL_IN, main-board:TestPoint_Pad_D1.0mm_Tight, B.Cu at (6.00, 95.0)
- added TP106: TP_NEUTRAL, main-board:TestPoint_Pad_D1.0mm_Tight, B.Cu at (25.5, 59.5)
- added TP107: TP_NEUTRAL_IN_V, main-board:TestPoint_Pad_D1.0mm_Tight, B.Cu at (9.00, 95.0)
- added TP108: TP_NEUTRAL_V, main-board:TestPoint_Pad_D1.0mm_Tight, B.Cu at (26.5, 57.0)
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
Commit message: main-board: placement candidate 2 [SOL-HW-MAIN-BOARD-PROVEN-AND-LAID-OUT.C7]
Candidate 1 with the zero-crossing detector brought into mains and the pump column rearranged to hold it
(moves by KiCad's Python, refilled and saved twice, byte-identical):

- U602 (55, 23.82) r90 across the opto column's mains/low-voltage border between U711 and U701, mains pins
  facing the triacs; T711 and U711 up 1.6 mm; R805 (63.2, 11.5) r90; Q701 (66, 35.5) r90 and R712
  (64, 39.5) into the low-voltage rectangle below the column; TP404 (88.25, 34.5);
- gate resistors to the tab side: R704 (36.2, 33.275), R705 (31.3, 33.275), R714 (36.3, 15.6),
  R715 (31.4, 15.6), all r180; TP702 (36, 46.75), TP712 (45, 23.25); C711 (38, 10.4);
- R630 (24, 40) beside RT301's LINE pin, R631 (19.5, 31.6) r180, TP103 (14.5, 40.6); TP630 (62.25, 25);
- F711 (30.4, 24.5), clearing R706 by 2.6 mm; R601 (25.6, 73.4) r-90, R602 (27.65, 79.3), R603
  (35.55, 79.5), TP102 (12.6, 94.6), clearing F731 and TP101 at the pollution degree 2 figures.

Every part inside its regions, no courtyard overlap, test pads 2.5 mm apart and 1 mm from every
courtyard, all eight tab plugs clear, mains pad-to-pad spacing at the pollution degree 2 figures except
the LINE/LINE1 10 mm pairs the slots hold by path.

Co-Authored-By: Claude Sonnet 5.5 <noreply@anthropic.com>
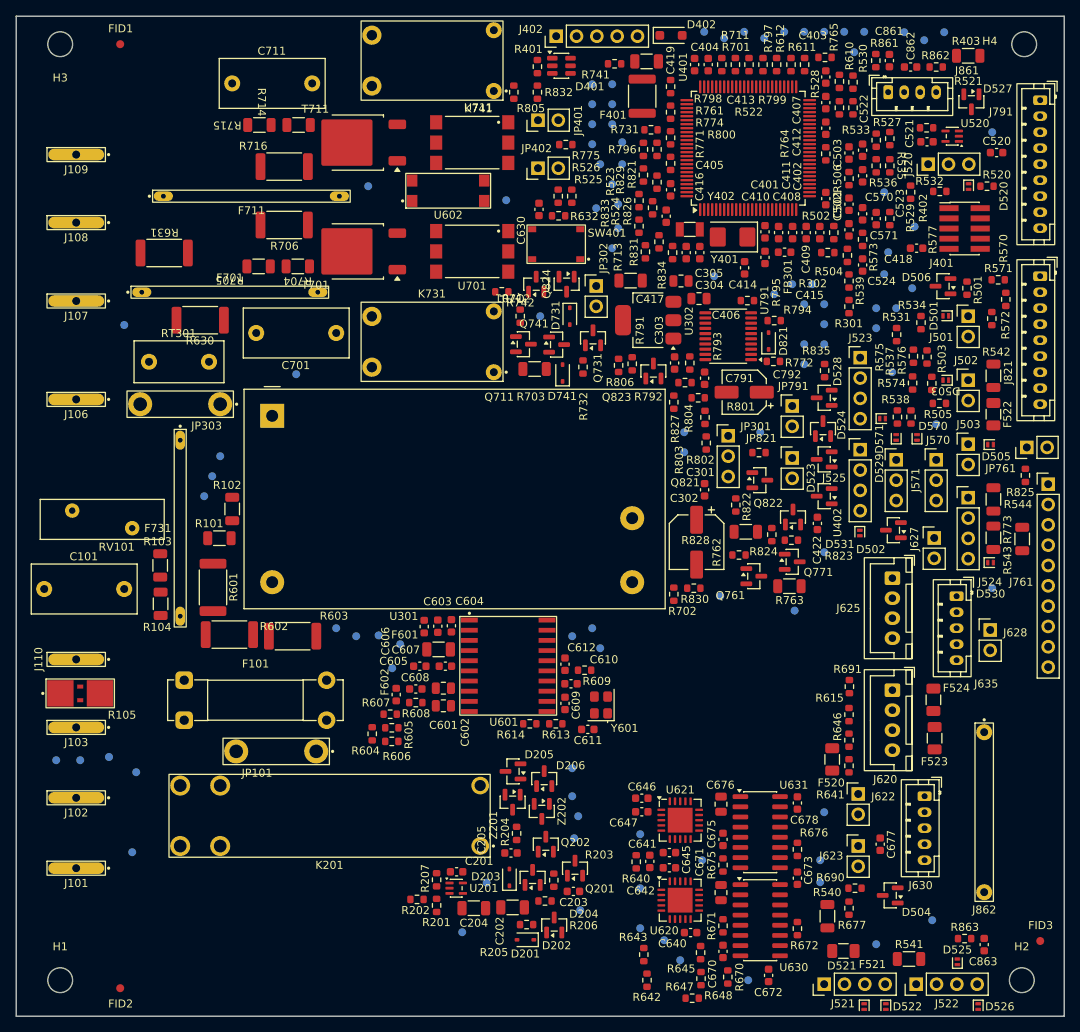
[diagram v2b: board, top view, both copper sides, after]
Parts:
- moved U602 98.7 mm to (55.0, 23.8)
- moved R631 95.4 mm to (19.5, 31.6), turned to 180 degrees
- moved TP630 91.5 mm to (62.2, 25.0)
- moved TP103 83.2 mm to (14.5, 40.6)
- moved R630 83.0 mm to (24.0, 40.0)
- moved TP404 22.8 mm to (88.2, 34.5)
- moved R705 20.5 mm to (31.3, 33.3), turned to 180 degrees
- moved R715 19.5 mm to (31.4, 15.6), turned to 180 degrees
- moved R712 14.2 mm to (64.0, 39.5)
- moved TP702 13.8 mm to (36.0, 46.8)
- moved TP712 11.8 mm to (45.0, 23.2)
- moved R704 11.7 mm to (36.2, 33.3), turned to 180 degrees
- moved Q701 10.7 mm to (66.0, 35.5), turned to 90 degrees
- moved R714 9.71 mm to (36.3, 15.6), turned to 180 degrees
- moved C711 3.54 mm to (38.0, 10.4)
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
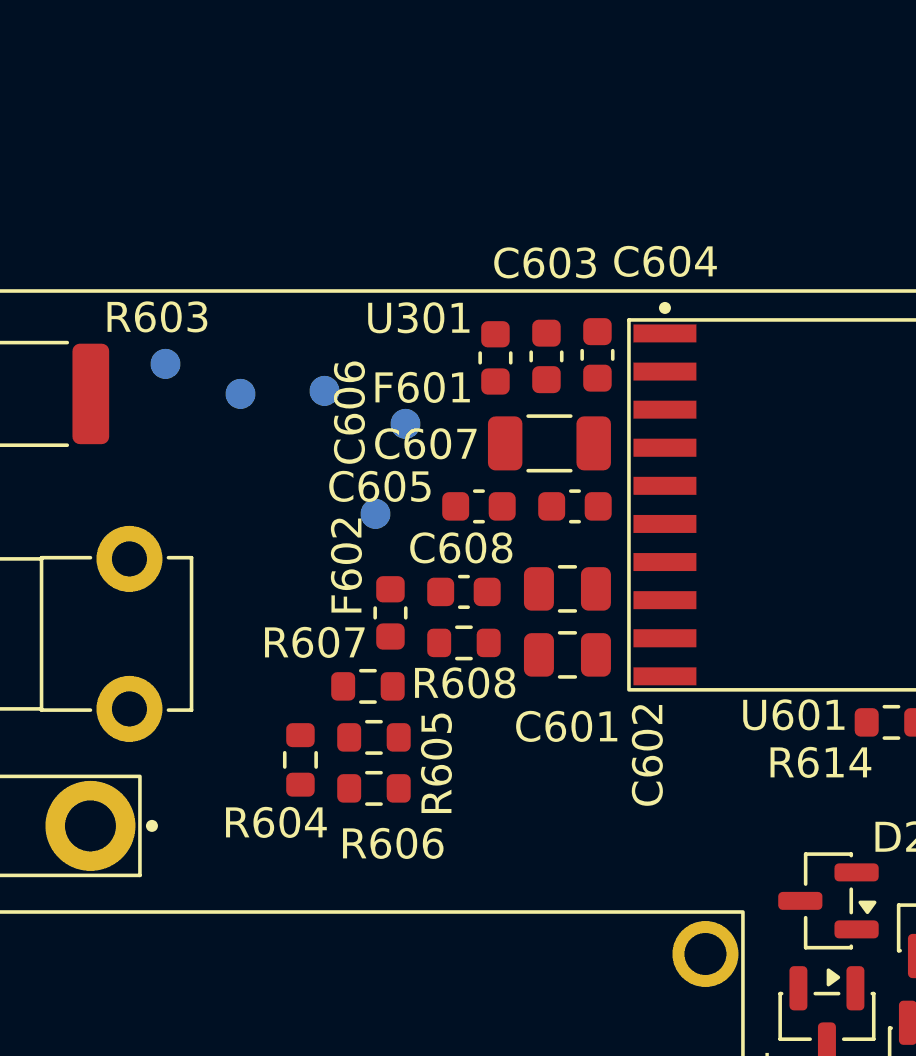
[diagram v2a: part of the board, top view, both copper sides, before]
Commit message: main-board: placement candidate 3 [SOL-HW-MAIN-BOARD-PROVEN-AND-LAID-OUT.C7]
Candidate 2 with the U601 measurement cluster re-placed as one placement-only change
(moves by KiCad's Python, refilled and saved twice, byte-identical): C601-C608, F601, F602,
R604-R608 and TP605-TP608 move or turn; no other part moves and no track, via or pour is drawn.

Co-Authored-By: Claude Sonnet 5.5 <noreply@anthropic.com>
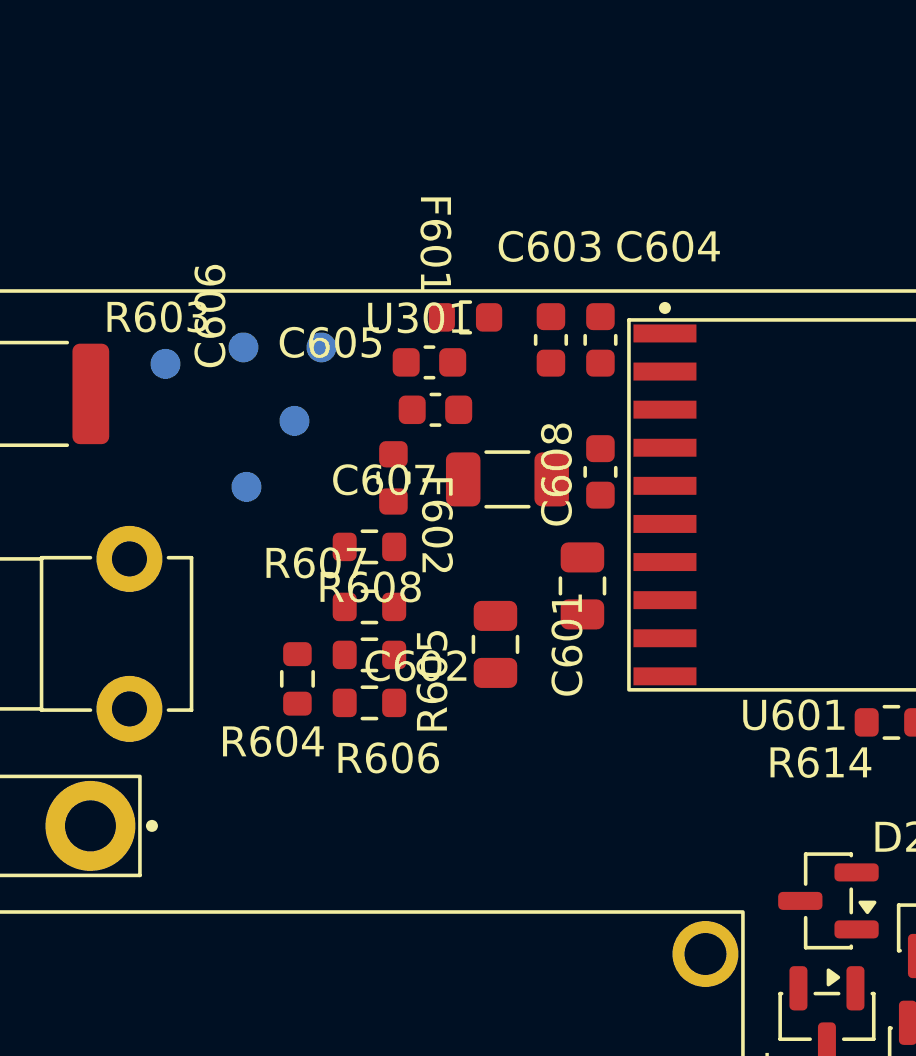
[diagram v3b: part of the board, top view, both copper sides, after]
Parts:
- moved C608 6.06 mm to (55.5, 82.1), turned to -90 degrees
- moved C606 5.66 mm to (50.0, 80.0)
- moved C605 5.08 mm to (49.8, 78.5)
- moved F602 4.50 mm to (48.6, 82.3), turned to 90 degrees
- moved R608 4.49 mm to (47.8, 84.6)
- moved TP606 4.39 mm to (43.7, 82.6)
- moved TP608 3.70 mm to (45.3, 80.4)
- moved R606 2.85 mm to (47.8, 89.8)
- moved R605 2.75 mm to (47.8, 88.2)
- moved R604 2.70 mm to (45.4, 89.0)
- moved R607 2.65 mm to (47.8, 86.6)
- moved C601 2.43 mm to (52.0, 87.8), turned to -90 degrees
- moved C607 1.84 mm to (52.4, 82.3)
- moved F601 1.68 mm to (51.0, 77.0), turned to 180 degrees
- moved TP605 1.55 mm to (43.6, 78.0)
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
